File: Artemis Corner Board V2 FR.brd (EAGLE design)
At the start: 132.4 x 63.1 mm, 59 parts, among them U1 TPS562219, U2 TM4C1231C3PM, U21 LM1085IS, U3 TPS562219, U4 MCP2562FD

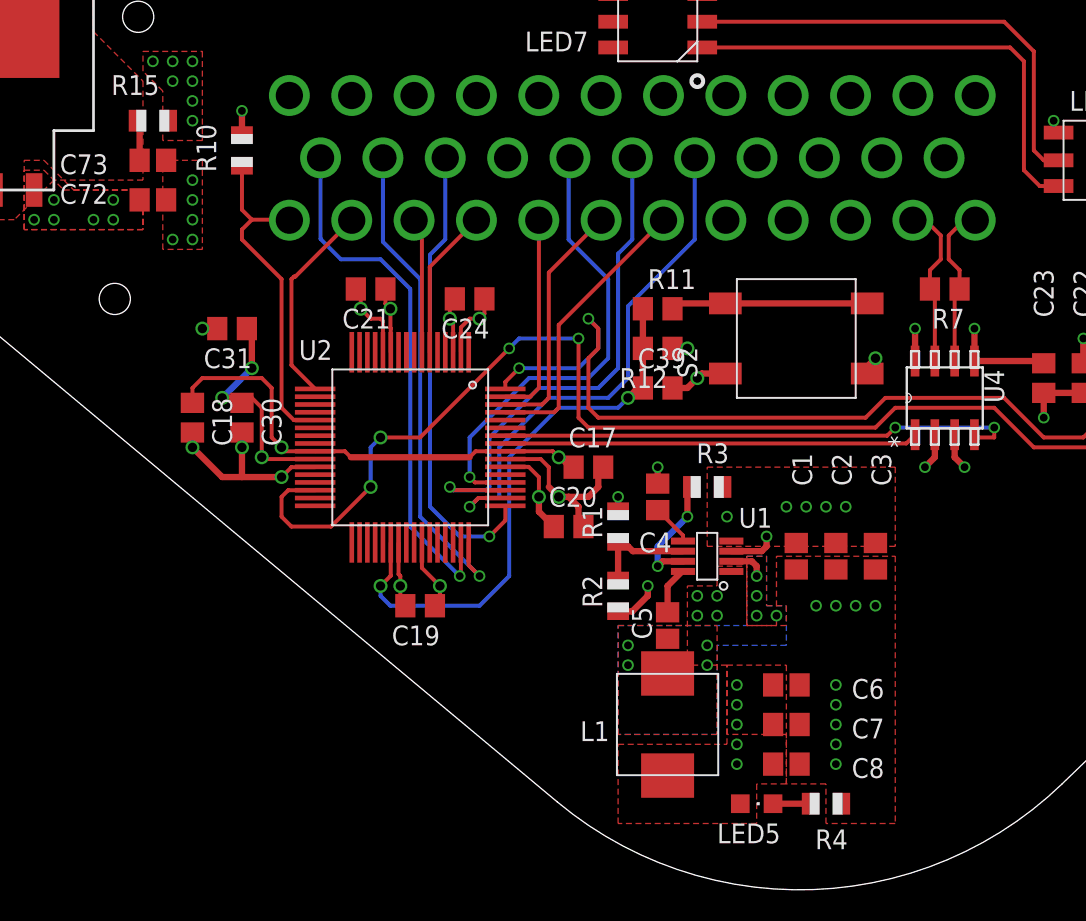
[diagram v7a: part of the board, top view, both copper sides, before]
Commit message: Added Series Termination Resistors
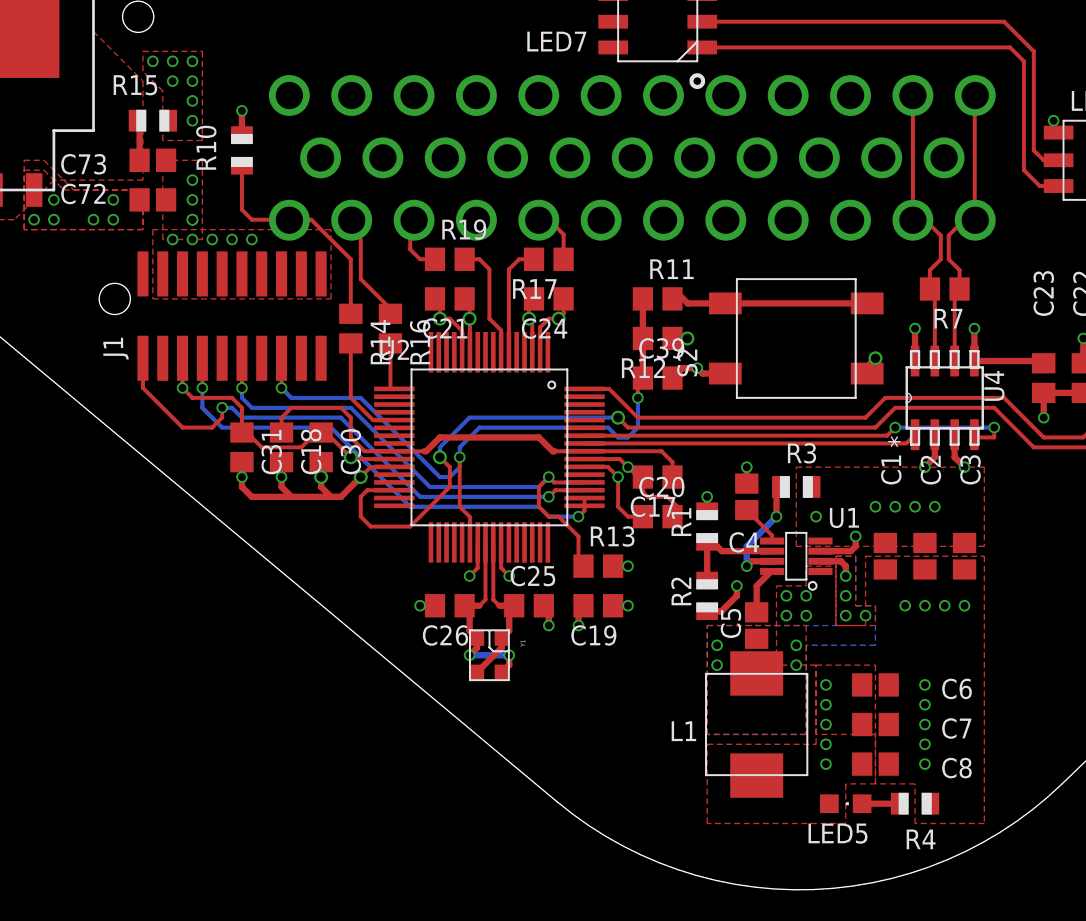
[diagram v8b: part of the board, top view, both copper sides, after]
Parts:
- added C25, C26: 12pF, rcl:C0805
- added J1: (no value), FormE:SAMTEC-FTR-DUALROW
- added R13: 1K, rcl:R0805
- added R14, R16, R17, R19: 22, rcl:R0805
- added Y1: NX3225GA, FormE:4-SMD
- moved C19 11.4 mm to (6.99, -27.3)
- moved C31 7.65 mm to (-15.9, -17.1), turned to 270 degrees
- moved C18 6.02 mm to (-13.3, -17.1)
- moved C20 5.75 mm to (10.8, -21.6)
- moved C4 5.72 mm to (16.5, -20.3)
- moved C1 5.71 mm to (25.4, -24.1)
- moved C2 5.71 mm to (27.9, -24.1)
- moved C3 5.71 mm to (30.5, -24.1)
- moved C5 5.71 mm to (17.1, -28.6)
- moved C6 5.71 mm to (24.8, -32.4)
- moved C7 5.71 mm to (24.8, -34.9)
- moved C8 5.71 mm to (24.8, -37.5)
- moved L1 5.71 mm to (17.1, -34.9)
- moved LED5 5.71 mm to (22.9, -40.0)
- moved R1 5.71 mm to (14.0, -22.2)
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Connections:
- removed net IR_SENSOR_1_ANALOG_OUT: H1.30, U2.61
- removed net IR_SENSOR_1_DIGITAL_IN: H1.19, U2.50
- removed net IR_SENSOR_1_DIGITAL_OUT: H1.15, U2.49
- removed net IR_SENSOR_2_ANALOG_OUT: H1.29, U2.62
- removed net IR_SENSOR_2_DIGITAL_IN: H1.18, U2.51
- removed net IR_SENSOR_2_DIGITAL_OUT: H1.14, U2.48
- removed net IR_SENSOR_3_ANALOG_OUT: H1.28, U2.63
- removed net IR_SENSOR_3_DIGITAL_IN: H1.17, U2.52
- removed net IR_SENSOR_3_DIGITAL_OUT: H1.13, U2.47
- new net DAMPER_POS_OUT_TR: R16.2, U2.17
- new net N$5: C25.1, U2.41, Y1.1, Y1.3
- new net N$6: C26.1, U2.40, Y1.2, Y1.4
- new net STRAIN_GADGE_VOLTMETER_IN_0_TR: R17.2, U2.6
- new net STRAIN_GADGE_VOLTMETER_IN_1_TR: R19.2, U2.7
- new net TCK: J1.11, R13.1, U2.52
- new net TDI: J1.3
- new net TDO: J1.7, U2.49, U2.50
- new net TMS: J1.1, U2.51
- new net TRCLK: U2.31
- new net WHEEL_SPEED_OUT_TR: R14.2, U2.21
- net +12V: no longer H1.4, H1.5, H1.6
- net +3V3: now also J1.5
- net +5V: now also H1.10
- net DAMPER_POS_OUT: now also R16.1; no longer U2.17
- net GND: now also C25.2, C26.2, H1.19, J1.10, J1.12, J1.16, J1.20, J1.4, J1.8, R13.2
- net MCU_RESET: now also J1.15
- net PROGRAMMING_CAN_N: now also H1.12
- net PROGRAMMING_CAN_P: now also H1.11
- net STRAIN_GADGE_VOLTMETER_IN_0: now also H1.28, R17.1; no longer H1.27, U2.6
- net STRAIN_GADGE_VOLTMETER_IN_1: now also R19.1; no longer U2.7
- net WHEEL_SPEED_OUT: now also R14.1; no longer U2.21
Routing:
- net TCK: track 0.00 -> 34.8 mm, vias 0 -> 2
- net TMS: track 0.00 -> 34.7 mm, vias 0 -> 2
- net IR_SENSOR_3_DIGITAL_OUT: track 34.2 -> 0.00 mm, vias 1 -> 0
- net IR_SENSOR_1_DIGITAL_IN: track 33.9 -> 0.00 mm, vias 1 -> 0
- net IR_SENSOR_2_DIGITAL_IN: track 33.5 -> 0.00 mm, vias 1 -> 0
- net IR_SENSOR_2_DIGITAL_OUT: track 31.8 -> 0.00 mm, vias 1 -> 0
- net TDO: track 0.00 -> 31.6 mm, vias 0 -> 2
- net IR_SENSOR_3_DIGITAL_IN: track 29.9 -> 0.00 mm, vias 1 -> 0
- net IR_SENSOR_1_DIGITAL_OUT: track 29.8 -> 0.00 mm, vias 1 -> 0
- net IR_SENSOR_1_ANALOG_OUT: track 18.4 -> 0.00 mm
- net IR_SENSOR_2_ANALOG_OUT: track 15.8 -> 0.00 mm
- net SPI_SCARY_LED_TRANSMIT: track 59.5 -> 44.5 mm, vias 2 -> 0
- net IR_SENSOR_3_ANALOG_OUT: track 13.2 -> 0.00 mm
- net N$6: track 0.00 -> 12.6 mm, vias 0 -> 2
- net SPI_SCARY_LED_CLOCK: track 78.1 -> 66.7 mm, vias 4 -> 2
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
